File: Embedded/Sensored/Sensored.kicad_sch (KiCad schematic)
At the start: 15 parts, among them J1 Casselation, J2 EPad, U1 ICM-20948, U3 BME280, U4 TLV74318PDQNR3

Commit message: Optimised JLCPCB Specific Parts
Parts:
- C1, C3, C4, C6, C8: LCSC C100072 -> C1525
- C11, C9: LCSC C107372 -> C52923
- C13: LCSC C412251 -> C15525
- R1, R2: LCSC C60490 -> C25744
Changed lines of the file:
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@@
 			)
 		)
-		(property "LCSC" "C60490"
+		(property "LCSC" "C25744"
 			(at 180.34 107.95 0)
 			(effects
@@
 			)
 		)
-		(property "LCSC" "C100072"
+		(property "LCSC" "C1525"
 			(at 130.81 105.41 0)
 			(effects
@@
 			)
 		)
-		(property "LCSC" "C100072"
+		(property "LCSC" "C1525"
 			(at 118.11 105.41 0)
 			(effects
@@
 			)
 		)
-		(property "LCSC" "C100072"
+		(property "LCSC" "C1525"
 			(at 80.01 134.62 0)
 			(effects
@@
 			)
 		)
-		(property "LCSC" "C107372"
+		(property "LCSC" "C52923"
 			(at 60.96 55.88 0)
 			(effects
@@
 			)
 		)
-		(property "LCSC" "C100072"
+		(property "LCSC" "C1525"
 			(at 67.31 107.95 0)
 			(effects
@@
 			)
 		)
-		(property "LCSC" "C60490"
+		(property "LCSC" "C25744"
 			(at 167.64 107.95 0)
 			(effects
@@
 			)
 		)
-		(property "LCSC" "C412251"
+		(property "LCSC" "C15525"
 			(at 106.68 55.88 0)
 			(effects
@@
 			)
 		)
-		(property "LCSC" "C100072"
+		(property "LCSC" "C1525"
 			(at 54.61 107.95 0)
 			(effects
@@
 			)
 		)
-		(property "LCSC" "C107372"
+		(property "LCSC" "C52923"
 			(at 96.52 55.88 0)
 			(effects

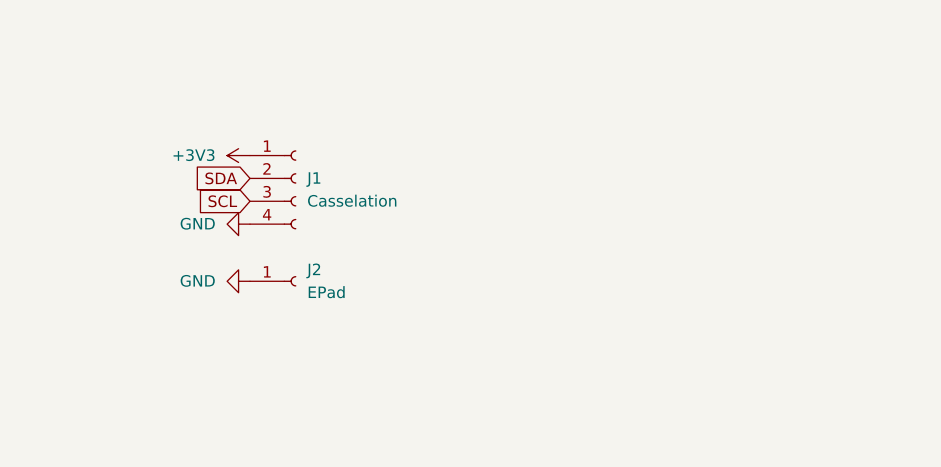
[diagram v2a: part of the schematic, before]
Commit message: Modified Outline & Component Placements for V2
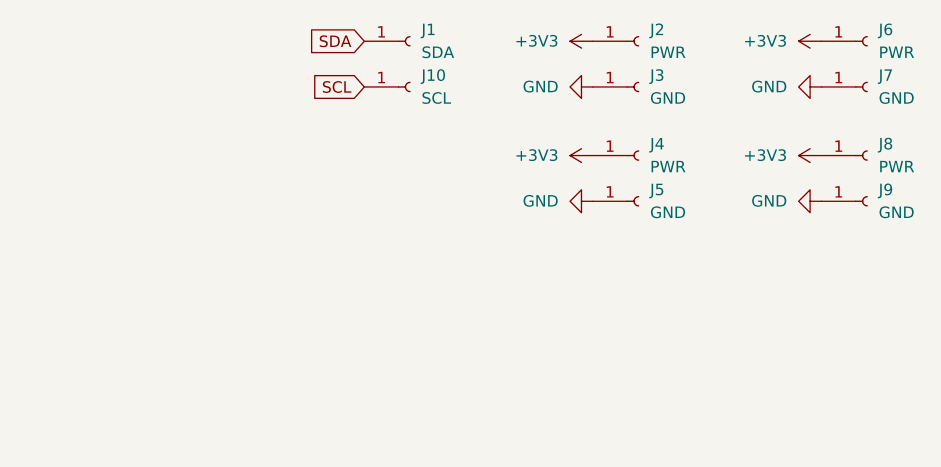
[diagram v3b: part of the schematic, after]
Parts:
- removed J1: Casselation, Simple_Connector:1mm_4P, symbol Connector:Conn_01x04_Socket
- added J1: SDA, Custom Connectors:1mm Pads, symbol Connector:Conn_01x01_Socket
- added J10: SCL, Custom Connectors:1mm Pads, symbol Connector:Conn_01x01_Socket
- added J3, J5, J7, J9: GND, Custom Connectors:1mm Pads, symbol Connector:Conn_01x01_Socket
- added J4, J6, J8: PWR, Custom Connectors:1mm Pads, symbol Connector:Conn_01x01_Socket
- J2: value EPad -> PWR; footprint Simple_Connector:1mm 3x3 Pad -> Custom Connectors:1mm Pads; now in the parts list
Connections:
- net +3V3: now also J2.1 (Pin_1), J4.1 (Pin_1), J6.1 (Pin_1), J8.1 (Pin_1)
- net GND: now also J3.1 (Pin_1), J5.1 (Pin_1), J7.1 (Pin_1), J9.1 (Pin_1); no longer J2.1 (Pin_1)
- net SCL: now also J10.1 (Pin_1)
- net SDA: now also J1.1 (Pin_1)

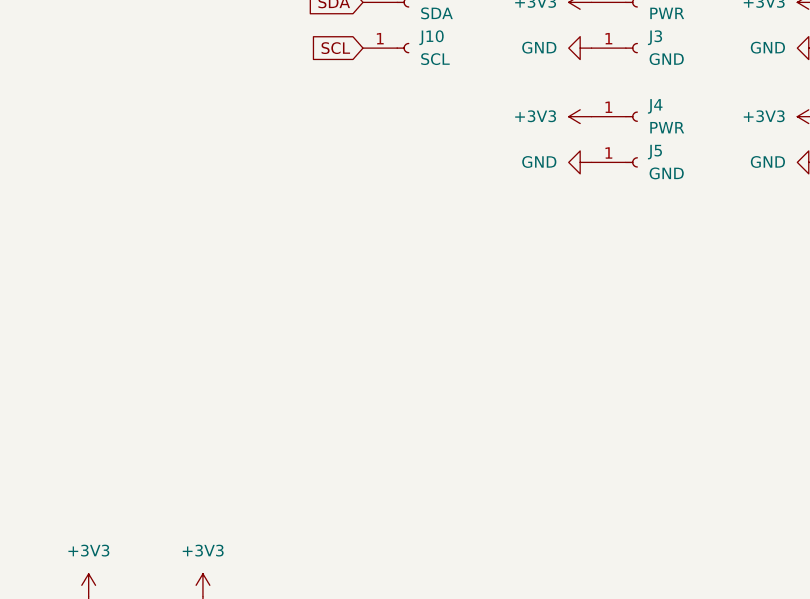
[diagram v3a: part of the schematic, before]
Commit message: Modified Component Placement & Added Adapting Pads
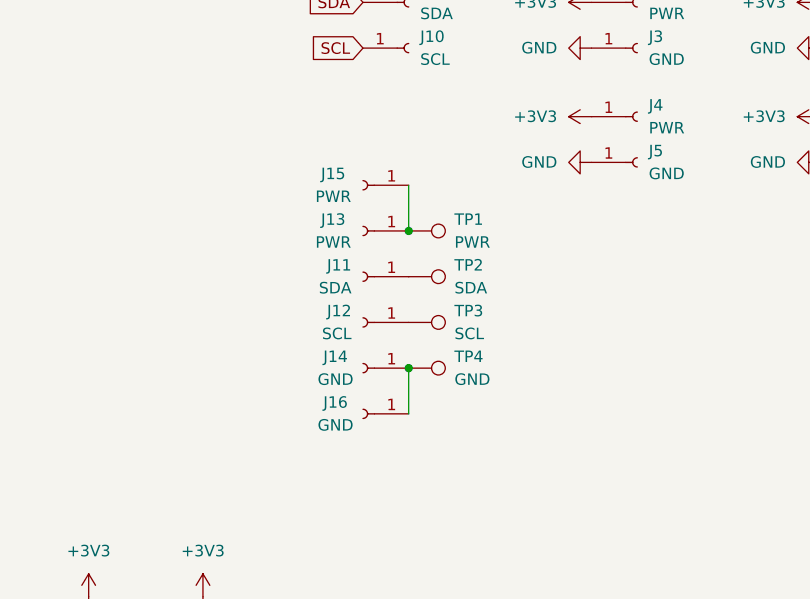
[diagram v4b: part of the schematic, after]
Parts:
- added J11: SDA, Custom Connectors:1mm Pads, symbol Connector:Conn_01x01_Socket
- added J12: SCL, Custom Connectors:1mm Pads, symbol Connector:Conn_01x01_Socket
- added J13, J15: PWR, Custom Connectors:1mm Pads, symbol Connector:Conn_01x01_Socket
- added J14, J16: GND, Custom Connectors:1mm Pads, symbol Connector:Conn_01x01_Socket
- added TP1: PWR, Connector_PinHeader_2.54mm:PinHeader_1x01_P2.54mm_Vertical, symbol Connector:TestPoint
- added TP2: SDA, Connector_PinHeader_2.54mm:PinHeader_1x01_P2.54mm_Vertical, symbol Connector:TestPoint
- added TP3: SCL, Connector_PinHeader_2.54mm:PinHeader_1x01_P2.54mm_Vertical, symbol Connector:TestPoint
- added TP4: GND, Connector_PinHeader_2.54mm:PinHeader_1x01_P2.54mm_Vertical, symbol Connector:TestPoint
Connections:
- new net: J14.1 (Pin_1), J16.1 (Pin_1), TP4.1
- new net: J13.1 (Pin_1), J15.1 (Pin_1), TP1.1
- new net: J12.1 (Pin_1), TP3.1
- new net: J11.1 (Pin_1), TP2.1

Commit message: Added Component Routing
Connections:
- net GNDE: now reaches J14.1 (Pin_1), J16.1 (Pin_1), TP4.1
- net +3V3E: now reaches J13.1 (Pin_1), J15.1 (Pin_1), TP1.1
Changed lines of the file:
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@@
 	)
 	(junction
+		(at 203.2 83.82)
+		(diameter 0)
+		(color 0 0 0 0)
+	)
+	(junction
 		(at 63.5 107.95)
 		(diameter 0)
@@
 		(color 0 0 0 0)
 	)
+	(junction
+		(at 203.2 58.42)
+		(diameter 0)
+		(color 0 0 0 0)
+	)
 	(no_connect
 		(at 73.66 127)
@@
 	)
 	(symbol
+		(lib_id "power:+3V3")
+		(at 203.2 58.42 0)
+		(unit 1)
+		(exclude_from_sim no)
+		(in_bom yes)
+		(on_board yes)
+		(dnp no)
+		(fields_autoplaced yes)
+		(property "Reference" "#PWR033"
+			(at 203.2 62.23 0)
+			(effects
+				(font
+					(size 1.27 1.27)
+				)
+				(hide yes)
+			)
+		)
+		(property "Value" "+3V3E"
+			(at 203.2 53.34 0)
+			(effects
+				(font
+					(size 1.27 1.27)
+				)
+			)
+		)
+		(property "Footprint" ""
+			(at 203.2 58.42 0)
+			(effects
+				(font
+					(size 1.27 1.27)
+				)
+				(hide yes)
+			)
+		)
+		(property "Datasheet" ""
+			(at 203.2 58.42 0)
+			(effects
+				(font
+					(size 1.27 1.27)
+				)
+				(hide yes)
+			)
+		)
+		(property "Description" "Power symbol creates a global label with name \"+3V3\""
+			(at 203.2 58.42 0)
+			(effects
+				(font
+					(size 1.27 1.27)
+				)
+				(hide yes)
+			)
+		)
+		(pin "1"
+		)
+		(instances
+			(project "Sensored"
+				(path "/83b90de2-6fa0-4a2d-8dd8-277ebe2ef879"
+					(reference "#PWR033")
+					(unit 1)
+				)
+			)
+		)
+	)
+	(symbol
 		(lib_id "Device:C")
 		(at 118.11 105.41 90)
@@
 					(unit 1)
 				)
+			)
+		)
+	)
+	(symbol
+		(lib_id "power:GND")
+		(at 203.2 83.82 0)
+		(unit 1)
+		(exclude_from_sim no)
+		(in_bom yes)
+		(on_board yes)
+		(dnp no)
+		(fields_autoplaced yes)
+		(property "Reference" "#PWR034"
+			(at 203.2 90.17 0)
+			(effects
+				(font
+					(size 1.27 1.27)
+				)
+				(hide yes)
+			)
+		)
+		(property "Value" "GNDE"
+			(at 203.2 88.9 0)
+			(effects
+				(font
+					(size 1.27 1.27)
+				)
+			)
+		)
+		(property "Footprint" ""
+			(at 203.2 83.82 0)
+			(effects
+				(font
+					(size 1.27 1.27)
+				)
+				(hide yes)
+			)
+		)
+		(property "Datasheet" ""
+			(at 203.2 83.82 0)
+			(effects
+				(font
+					(size 1.27 1.27)
+				)
+				(hide yes)
+			)
+		)
+		(property "Description" "Power symbol creates a global label with name \"GND\" , ground"
+			(at 203.2 83.82 0)
+			(effects
+				(font
+					(size 1.27 1.27)
+				)
+				(hide yes)
+			)
+		)
+		(pin "1"
+		)
+		(instances
+			(project "Sensored"
+				(path "/83b90de2-6fa0-4a2d-8dd8-277ebe2ef879"
+					(reference "#PWR034")
+					(unit 1)
+				)

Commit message: Added Orientation Marker
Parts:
- J13, J15, J2, J4, J6, J8, TP1: value PWR -> 3V3
- U1: footprint Sensor_Motion:InvenSense_QFN-24_3x3mm_P0.4mm -> Sensor_Motion:InvenSense_QFN-24_3x3mm_P0.4mm_NoMask
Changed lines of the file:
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@@
 			)
 		)
-		(property "Value" "PWR"
+		(property "Value" "3V3"
 			(at 255.27 52.0699 0)
 			(effects
@@
 			)
 		)
-		(property "Value" "PWR"
+		(property "Value" "3V3"
 			(at 194.818 59.69 0)
 			(effects
@@
 			)
 		)
-		(property "Footprint" "Sensor_Motion:InvenSense_QFN-24_3x3mm_P0.4mm"
+		(property "Footprint" "Sensor_Motion:InvenSense_QFN-24_3x3mm_P0.4mm_NoMask"
 			(at 60.96 154.94 0)
 			(effects
@@
 			)
 		)
-		(property "Value" "PWR"
+		(property "Value" "3V3"
 			(at 229.87 52.0699 0)
 			(effects
@@
 			)
 		)
-		(property "Value" "PWR"
+		(property "Value" "3V3"
 			(at 208.28 64.7699 90)
 			(effects
@@
 			)
 		)
-		(property "Value" "PWR"
+		(property "Value" "3V3"
 			(at 255.27 39.3699 0)
 			(effects
@@
 			)
 		)
-		(property "Value" "PWR"
+		(property "Value" "3V3"
 			(at 229.87 39.3699 0)
 			(effects
@@
 			)
 		)
-		(property "Value" "PWR"
+		(property "Value" "3V3"
 			(at 194.818 64.77 0)
 			(effects

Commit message: Verified LCSC Components
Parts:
- U1: footprint Sensor_Motion:InvenSense_QFN-24_3x3mm_P0.4mm_NoMask -> Sensor_Motion:InvenSense_QFN-24_3x3mm_P0.4mm
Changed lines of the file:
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@@
 			)
 		)
-		(property "Footprint" "Sensor_Motion:InvenSense_QFN-24_3x3mm_P0.4mm_NoMask"
+		(property "Footprint" "Sensor_Motion:InvenSense_QFN-24_3x3mm_P0.4mm"
 			(at 60.96 154.94 0)
 			(effects

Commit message: Modified Layout for JLCPCB
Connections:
- net +3V3E is gone; now on net +3V3: J13.1 (Pin_1), J15.1 (Pin_1), TP1.1
- net GNDE is gone; now on net GND: J14.1 (Pin_1), J16.1 (Pin_1), TP4.1
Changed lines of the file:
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@@
 			)
 		)
-		(property "Value" "+3V3E"
-			(at 203.2 53.34 0)
+		(property "Value" "+3V3"
+			(at 205.74 57.1499 0)
 			(effects
 				(font
 					(size 1.27 1.27)
 				)
+				(justify left)
 			)
 		)
@@
 			)
 		)
-		(property "Value" "GNDE"
-			(at 203.2 88.9 0)
+		(property "Value" "GND"
+			(at 205.74 85.0899 0)
 			(effects
 				(font
 					(size 1.27 1.27)
 				)
+				(justify left)
 			)
 		)
